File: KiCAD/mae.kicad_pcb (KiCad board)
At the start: 2 copper layers, 30 x 30 mm, 18 parts, among them K1 1437566-3 (FSMSM), K2 1437566-3 (FSMSM), X1 перемычка_разрывная

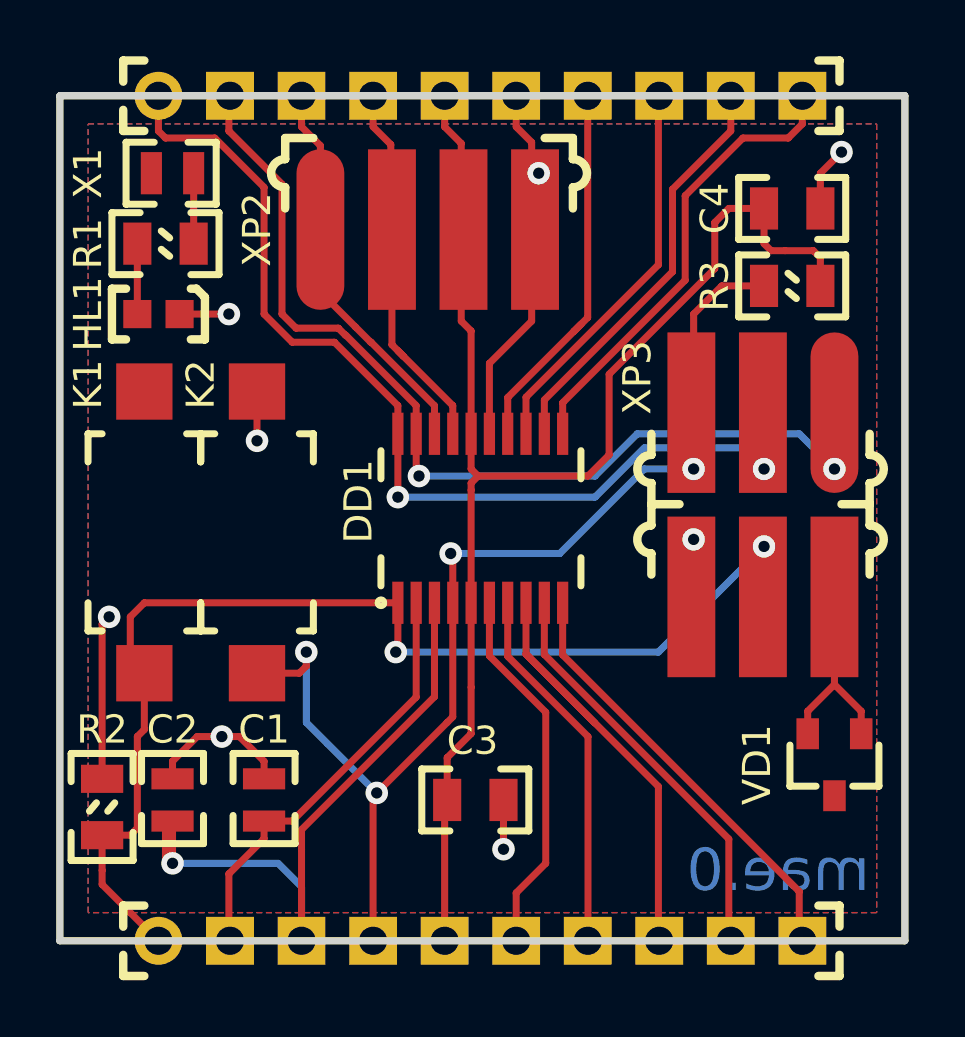
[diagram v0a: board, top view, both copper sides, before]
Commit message: добавлена шелкография сзади, переделана нумерация как ssop20
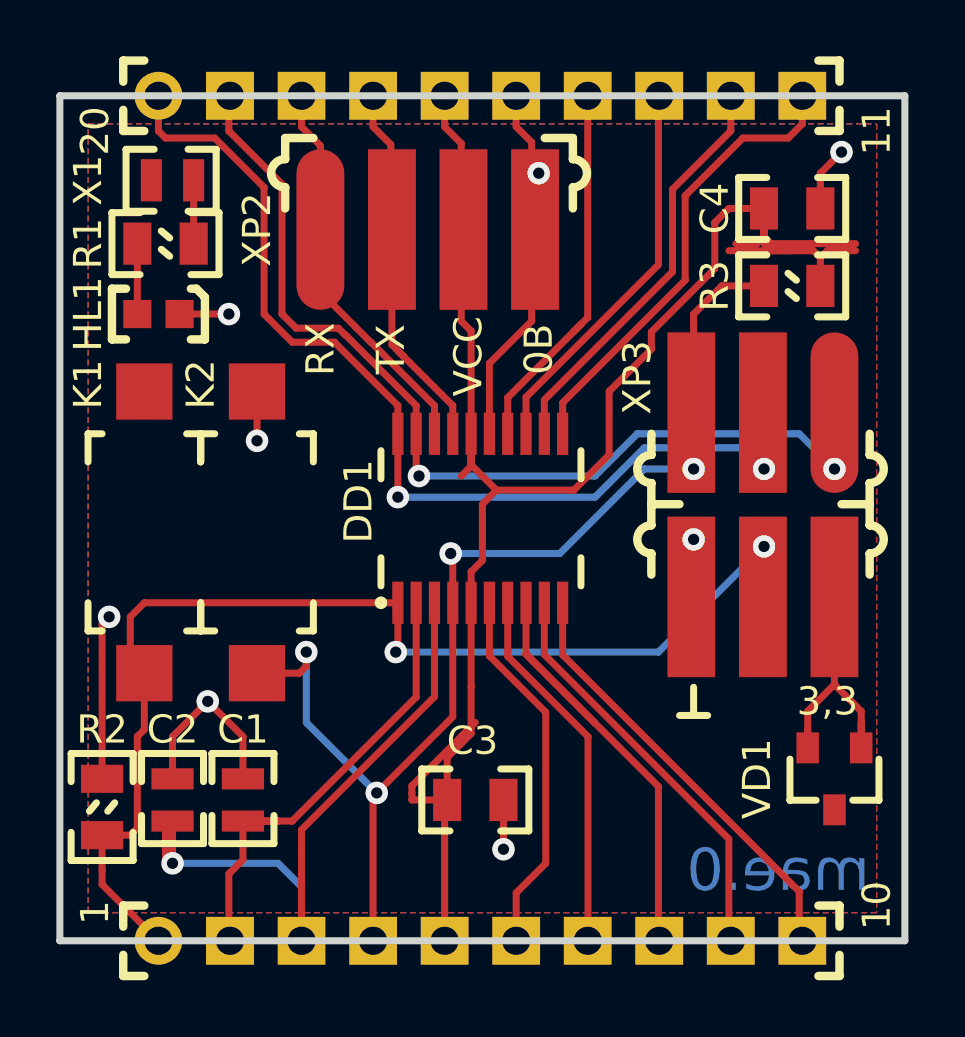
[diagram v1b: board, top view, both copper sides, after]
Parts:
- moved C1 0.75 mm to (99.8, 149.8)
- moved VD1 0.50 mm to (120.8, 148.2)
- moved X1 0.25 mm to (98.0, 127.0)
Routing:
- net /VCC: track 49.7 -> 65.8 mm
- net /VCCprog: track 9.40 -> 10.9 mm
- net /0В: track 28.2 -> 29.5 mm
- net /G4: track 14.9 -> 15.8 mm
- net Net-(R1-Pad1): track 2.50 -> 2.00 mm
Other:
- board text added: "0В"
- board text added: "1"
- board text added: "10"
- board text added: "11"
- board text added: "20"
- board text added: "3,3"
- board text added: "RX"
- board text added: "TX"
- board text added: "VCC"
- board text removed: "-разработка (PCB-design) -документация по ЕСКД -мелкосерийный монтаж -импортозамещение ( если надо :)"
- board text removed: "El.Nikitos@mail.ru +7(995)120-05-23 WhatsApp, Viber"

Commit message: добавлены герберы, на меди добавлены метки ключей
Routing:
- net /0В: track 29.5 -> 39.3 mm
- net (no net): track 0.00 -> 4.41 mm
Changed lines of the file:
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@@
     (thickness 1.6)
     (drawings 16)
-    (tracks 246)
+    (tracks 265)
     (zones 0)
     (modules 18)
@@
     (visible_elements 7FFFFFFF)
     (pcbplotparams
-      (layerselection 0x010fc_ffffffff)
+      (layerselection 0x010c0_ffffffff)
       (usegerberextensions false)
       (usegerberattributes false)
@@
       (outputformat 1)
       (mirror false)
-      (drillshape 1)
+      (drillshape 0)
       (scaleselection 1)
-      (outputdirectory ""))
+      (outputdirectory "GERBER/"))
   )
   (net 0 "")
@@
   (gr_line (start 123.25 124) (end 123.25 154) (layer Edge.Cuts) (width 0.25))
   (gr_line (start 93.25 124) (end 123.25 124) (layer Edge.Cuts) (width 0.25))
+  (segment (start 104.5 143) (end 104 142.5) (width 0.25) (layer F.Cu) (net 0))
+  (segment (start 104 142.5) (end 104 143.5) (width 0.25) (layer F.Cu) (net 0))
+  (segment (start 104 143.5) (end 104.5 143) (width 0.25) (layer F.Cu) (net 0))
+  (segment (start 108 148.75) (end 108 149.25) (width 0.25) (layer F.Cu) (net 0))
+  (segment (start 119.25 127.75) (end 119.25 128.25) (width 0.25) (layer F.Cu) (net 0))
+  (segment (start 97 149) (end 97.5 149) (width 0.25) (layer F.Cu) (net 0))
+  (segment (start 99.5 149) (end 100 149) (width 0.25) (layer F.Cu) (net 0))
   (segment (start 109.45 125.1) (end 110 125.65) (width 0.25) (layer F.Cu) (net 1))
   (segment (start 109.45 124) (end 109.45 125.1) (width 0.25) (layer F.Cu) (net 1))
@@
   (segment (start 99.75 146.75) (end 98.5 145.5) (width 0.25) (layer F.Cu) (net 1))
   (segment (start 99.75 148.25) (end 99.75 146.75) (width 0.25) (layer F.Cu) (net 1))
+  (segment (start 99.25 131.75) (end 99.25 132.75) (width 0.25) (layer F.Cu) (net 1))
+  (segment (start 99.25 132.75) (end 98.75 132.75) (width 0.25) (layer F.Cu) (net 1))
+  (segment (start 99.25 132.75) (end 99.75 132.75) (width 0.25) (layer F.Cu) (net 1))
+  (segment (start 112 127.75) (end 111.5 127.75) (width 0.25) (layer F.Cu) (net 1))
+  (segment (start 112 127.75) (end 112.5 127.75) (width 0.25) (layer F.Cu) (net 1))
+  (segment (start 112 126.75) (end 112 127.75) (width 0.25) (layer F.Cu) (net 1))
+  (segment (start 110.25 126.75) (end 112 126.75) (width 0.25) (layer F.Cu) (net 1))
+  (segment (start 115.75 139.75) (end 113.75 139.75) (width 0.25) (layer F.Cu) (net 1))
+  (segment (start 113.75 139.75) (end 113.75 140.75) (width 0.25) (layer F.Cu) (net 1))
+  (segment (start 113.75 140.75) (end 113.25 140.75) (width 0.25) (layer F.Cu) (net 1))
+  (segment (start 113.75 140.75) (end 114.25 140.75) (width 0.25) (layer F.Cu) (net 1))
   (segment (start 106.91 125.1) (end 107.5 125.69) (width 0.25) (layer F.Cu) (net 2))
   (segment (start 106.91 124) (end 106.91 125.1) (width 0.25) (layer F.Cu) (net 2))
@@
   (segment (start 109.8 134.7) (end 114.5 130) (width 0.25) (layer F.Cu) (net 16))
   (segment (start 114.5 130) (end 114.5 124) (width 0.25) (layer F.Cu) (net 16))
-  (segment (start 109.15 136) (end 109.15 134.71359) (width 0.25) (layer F.Cu) (net 17))
-  (segment (start 111.99 131.87359) (end 111.5 132.36359) (width 0.25) (layer F.Cu) (net 17))
-  (segment (start 111.99 124) (end 111.99 131.87359) (width 0.25) (layer F.Cu) (net 17))
-  (segment (start 111.5 132.36359) (end 111.75 132.11359) (width 0.25) (layer F.Cu) (net 17))
-  (segment (start 109.15 134.71359) (end 111.5 132.36359) (width 0.25) (layer F.Cu) (net 17))
+  (segment (start 111.99 125) (end 112 125) (width 0.25) (layer F.Cu) (net 17))
+  (segment (start 111.99 124) (end 111.99 125) (width 0.25) (layer F.Cu) (net 17))
+  (segment (start 112 125) (end 113 126) (width 0.25) (layer F.Cu) (net 17))
+  (segment (start 113 126) (end 113 130.75) (width 0.25) (layer F.Cu) (net 17))
+  (segment (start 109.15 134.6) (end 113 130.75) (width 0.25) (layer F.Cu) (net 17))
+  (segment (start 109.15 136) (end 109.15 134.6) (width 0.25) (layer F.Cu) (net 17))
   (segment (start 104.37 125.1) (end 105 125.73) (width 0.25) (layer F.Cu) (net 18))
   (segment (start 104.37 124) (end 104.37 125.1) (width 0.25) (layer F.Cu) (net 18))
